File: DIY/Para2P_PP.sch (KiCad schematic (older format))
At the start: 11 parts, among them J1 Atari_SEGA_DE9, J2 Atari_SEGA_DE9, J3 DB25_Male, U1 74AHCT125N, U2 74AHCT125N, U3 74AHCT125N, U4 CD74HC4053E

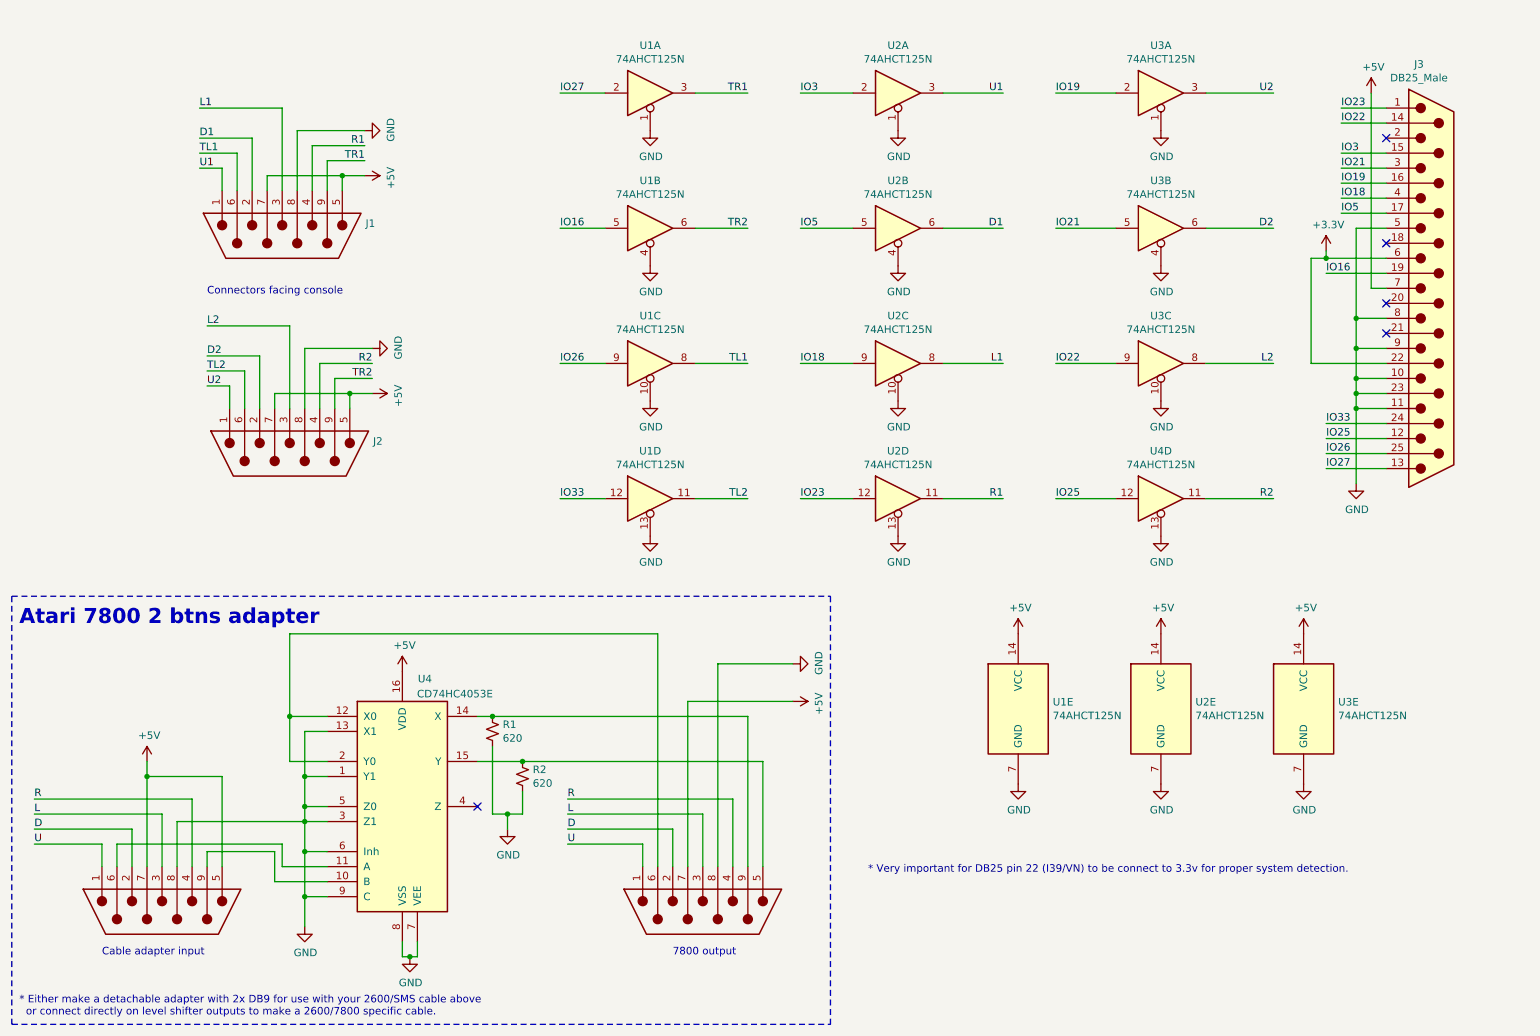
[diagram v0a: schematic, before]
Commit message: Simplify parallel schematics
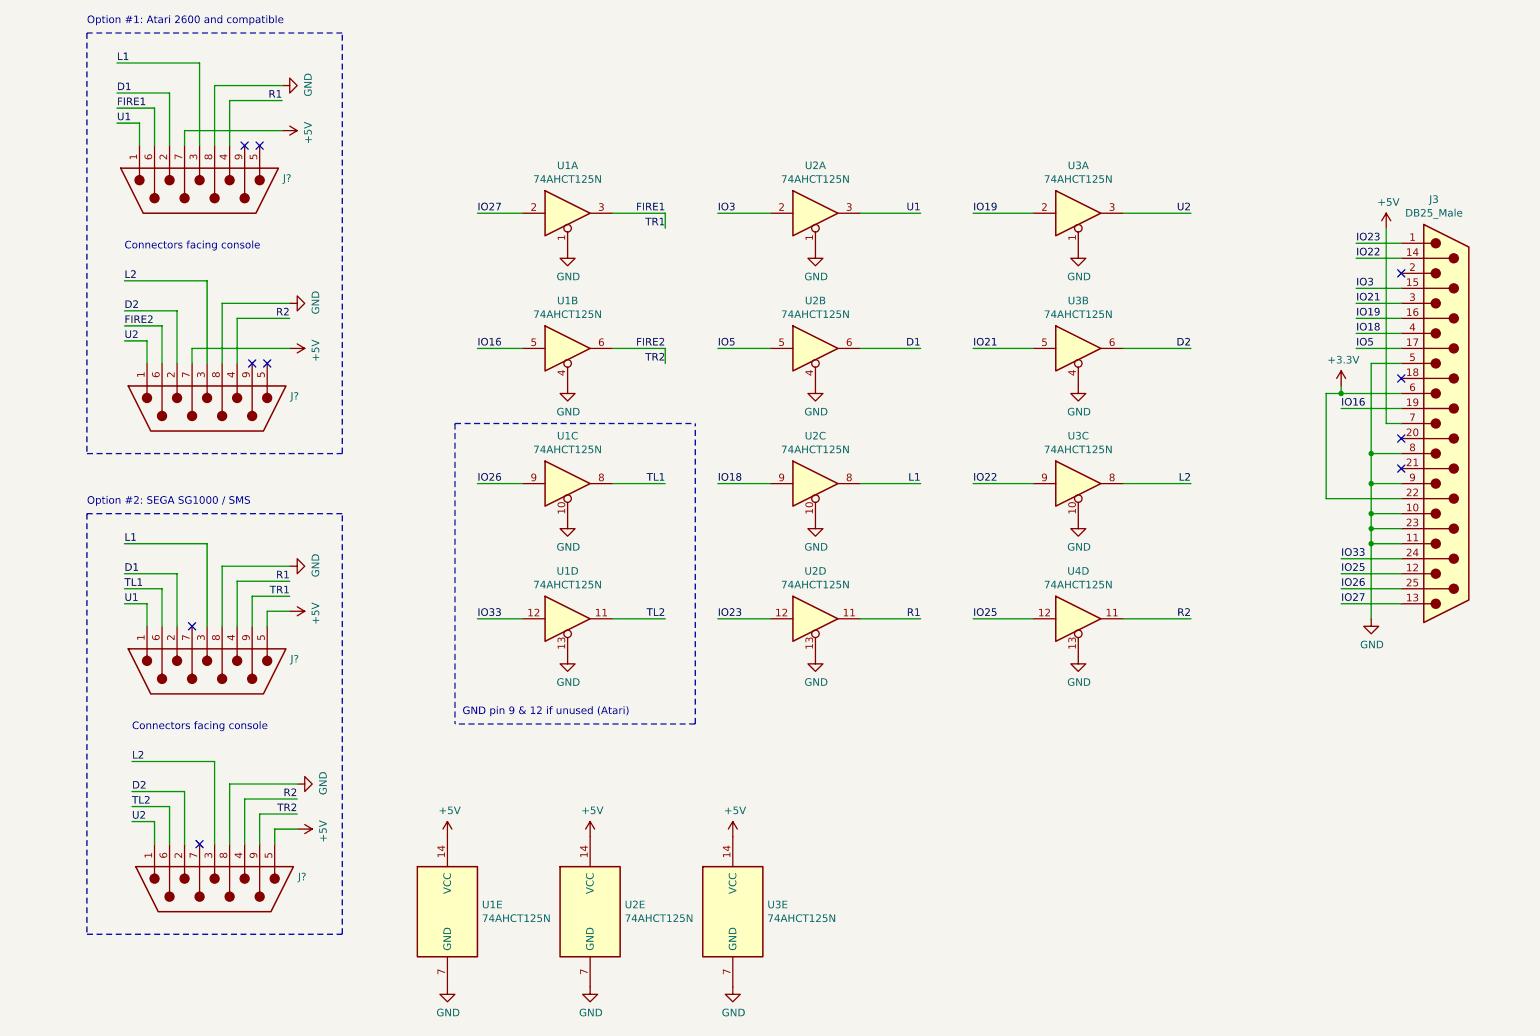
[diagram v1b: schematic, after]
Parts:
- removed J1, J2, J? (x2): Atari_SEGA_DE9, symbol Connector_Gaming:Atari_SEGA_DE9
- removed R1, R2: 620, symbol Device:R_Small_US
- removed unit 1 of U4
- added J? (x4): Atari_SEGA_DE9, symbol Connector_Gaming:Atari_SEGA_DE9
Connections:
- net +5V: now also J?.5, J?.5, J?.7, J?.7
- net D1: now also J?.2, J?.2
- net D2: now also J?.2, J?.2
- net GND: now also J?.8, J?.8, J?.8, J?.8
- net L1: now also J?.3, J?.3
- net L2: now also J?.3, J?.3
- net R1: now also J?.4, J?.4
- net R2: now also J?.4, J?.4
- net TL1: now also J?.6
- net TL2: now also J?.6
- net U1: now also J?.1, J?.1
- net U2: now also J?.1, J?.1
- net TR1 renamed FIRE1
- net FIRE1: now also J?.6, J?.9
- net TR2 renamed FIRE2
- net FIRE2: now also J?.6, J?.9
- no-connect marks 5 -> 10
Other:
- note added: "GND pin 9 & 12 if unused (Atari)"
- note added: "Option #1: Atari 2600 and compatible"
- note added: "Option #2: SEGA SG1000 / SMS"
- note removed: "* Either make a detachable adapter with 2x DB9 for use with your 2600/SMS cable above\n or connect directly on level shifter outputs to make a 2600/7800 specific cable."
- note removed: "* Very important for DB25 pin 22 (I39/VN) to be connect to 3.3v for proper system detection."
- note removed: "7800 output"
- note removed: "Atari 7800 2 btns adapter"
- note removed: "Cable adapter input"
- moved on the sheet: J3, U1A, U1B, U1C, U1D, U1E, U2A, U2B, U2C, U2D, U2E, U3A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
